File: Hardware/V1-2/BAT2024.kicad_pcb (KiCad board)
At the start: 2 copper layers, 60 x 60 mm, 49 parts, among them IC1 BGM220PC22WGA2R, IC2 EEPROM_M95P16-IXMNT_E, IC3 LED-Driver_LP55231SQX_NOPB, J1 USB4125-GF-A, J2 Conn_ARM_SWD_TagConnect_TC203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, Q1 SSM3J334R,LF, U1 MIC5504-3.3YM5, U2 BQ21040DBVR

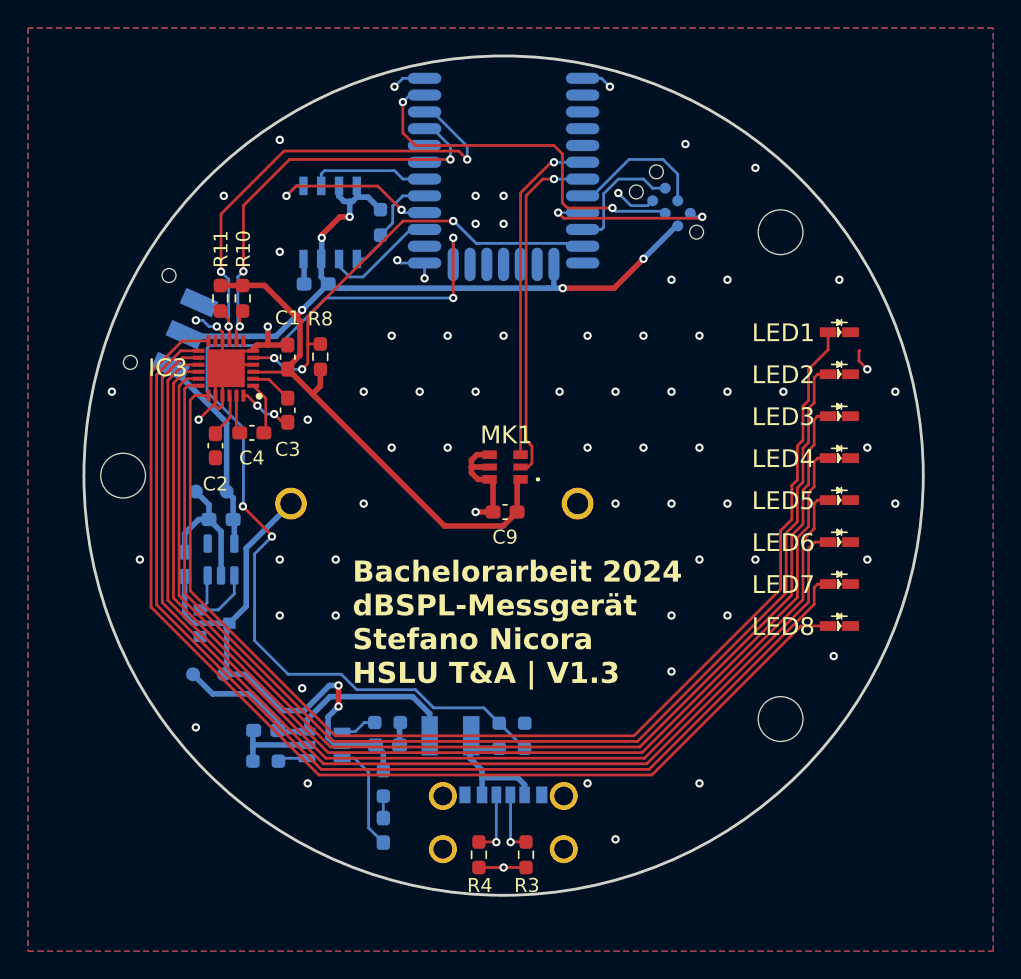
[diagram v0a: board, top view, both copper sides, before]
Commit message: Add V1-3 of PCB. See changelog for more information
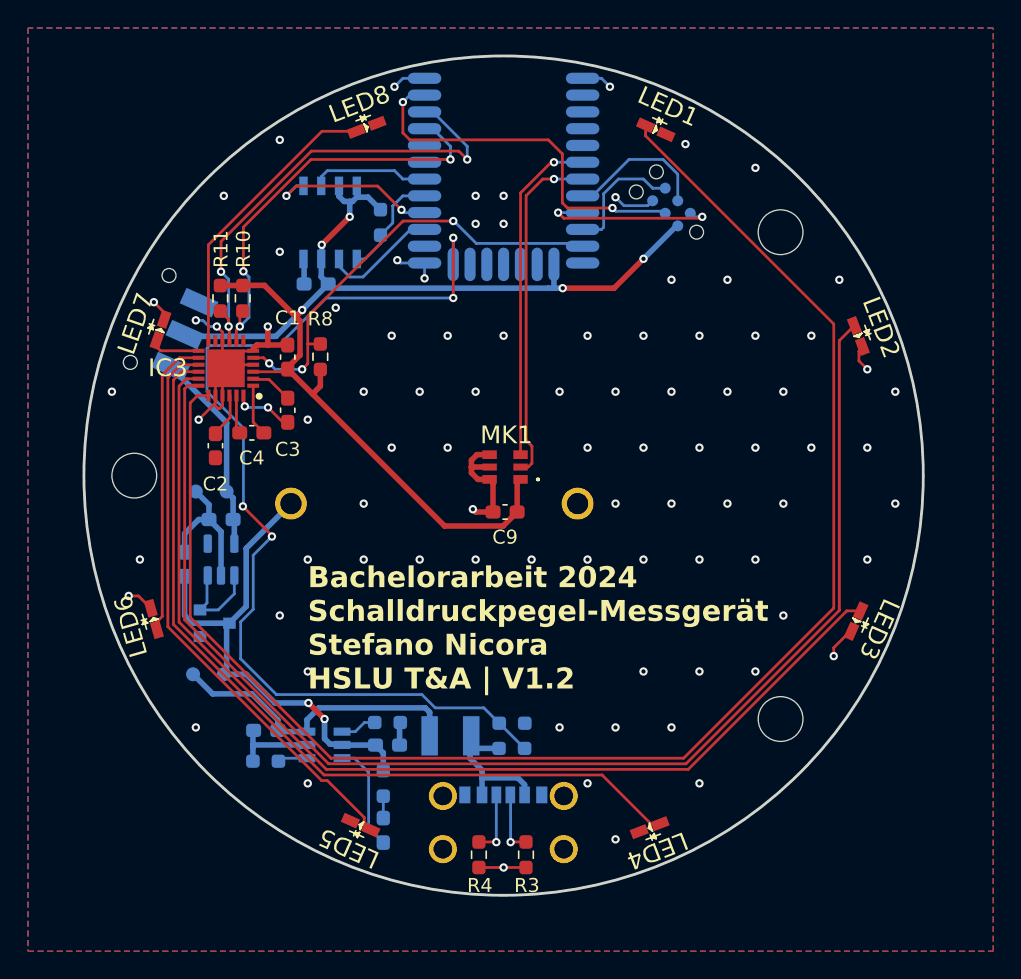
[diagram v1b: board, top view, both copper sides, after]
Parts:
- moved LED7 51.8 mm to (89.7, 46.9), turned to -109 degrees
- moved LED6 49.3 mm to (89.2, 67.6), turned to -74 degrees
- moved LED8 49.1 mm to (104.4, 32.4), turned to -159 degrees
- moved LED5 41.4 mm to (104.0, 82.3), turned to -24 degrees
- moved LED4 29.7 mm to (124.7, 82.5), turned to 21 degrees
- moved LED1 19.5 mm to (125.1, 32.6), turned to 156 degrees
- moved LED3 14.7 mm to (139.4, 67.7), turned to 66 degrees
- moved LED2 3.05 mm to (139.6, 47.3), turned to 111 degrees
- moved H3 0.80 mm to (87.8, 57.3)
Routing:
- net /LED7: track 79.2 -> 3.57 mm
- net /LED6: track 80.4 -> 21.5 mm
- net /LED8: track 79.6 -> 20.8 mm
- net /LED5: track 81.4 -> 41.0 mm
- net /LED1: track 85.7 -> 111.6 mm
- net /LED4: track 82.6 -> 60.2 mm
- net /LED2: track 84.8 -> 94.0 mm
- net /LED3: track 83.7 -> 76.3 mm
- net GND: track 65.3 -> 71.5 mm, vias 70 -> 86
- net +BATT: track 40.2 -> 36.3 mm
- net /Charge: track 71.1 -> 73.3 mm
- net /I2C_SCL: track 35.4 -> 34.2 mm
- net /I2C_SDA: track 30.7 -> 30.0 mm
- net VCC: track 22.8 -> 22.2 mm
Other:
- board text added: "Bachelorarbeit 2024 Schalldruckpegel-Messgerät Stefano Nicora HSLU T&A | V1.2"
- board text removed: "Bachelorarbeit 2024 dBSPL-Messgerät Stefano Nicora HSLU T&A | V1.3"
